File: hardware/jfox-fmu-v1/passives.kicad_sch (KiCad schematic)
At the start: 38 parts, among them X1 16MHz, X2 32.768kHz

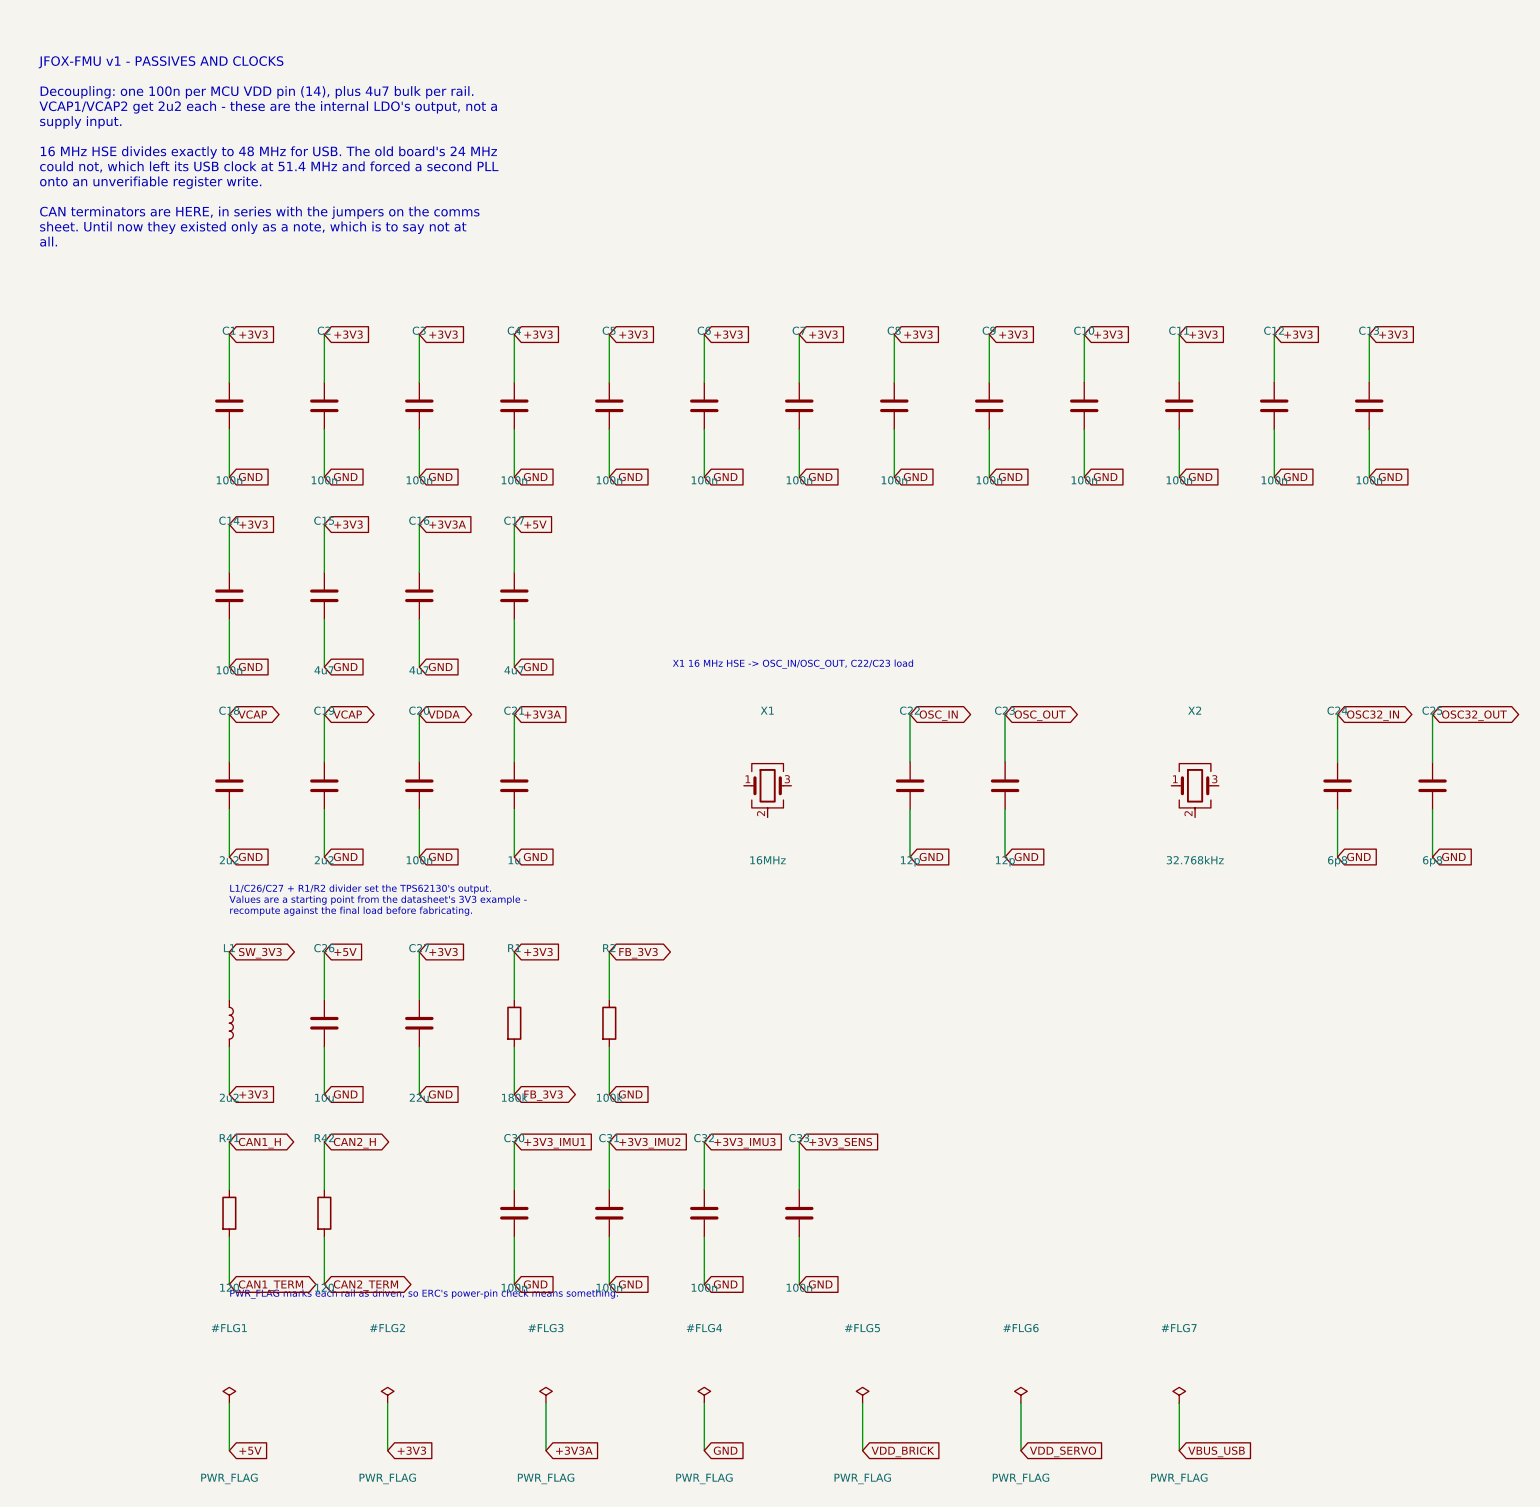
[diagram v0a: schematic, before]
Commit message: A4 title-blocked sheets, and the 25 power pins that were never wired
Every sheet now carries a title block naming JFOX Aircraft Co., Ltd., with a
per-sheet title, revision, date and the notes that used to float as loose text.

A4 PORTRAIT, not landscape, and not by preference. The STM32H753IITx symbol is
a single unit - KiCad's library gives it only _0_1 body and _1_1 pin
sub-symbols, so it cannot be split across pages - and its 176 pins span
231.1 mm. A4 landscape offers about 180 mm of usable height and would cut the
MCU in half. Portrait offers 237 mm. The part fits with 2 mm to spare, which
is why the page margin is 2 mm: it is the largest margin that still holds an
LQFP176, not a number chosen for looks.

The frame geometry was measured, not assumed - an empty A4 portrait sheet
plotted through kicad-cli, frame read off the SVG at 12,12 -> 198,285 with the
title block claiming x >= 90, y >= 253.

Three defects the work surfaced, in rising order of how much they mattered:

Every sheet had content at negative coordinates, off the page entirely, where
KiCad edits it happily and the plotter crops it away. Nothing had complained
because nothing was looking. fit() now translates each sheet into the drawable
area and refuses - loudly - to emit one that does not fit, because a schematic
that is silently cropped lies about the board.

fit() then passed the power sheet while its rightmost label sat 8.6 mm past
the frame. A global label's angle is the direction its CONNECTION faces, so
the text runs the opposite way; reading it the intuitive way put every
estimated extent on the wrong side of its anchor. That is worse than not
estimating: it reports "inside the frame" precisely when labels hang off it.
Caught by measuring KiCad's own plotted geometry instead of trusting the
estimate - which is what check_fmu_sheets.py now does on every sheet, with
--exclude-drawing-sheet so only the circuit is measured.

And centring the sheets by (SAFE_W - w) / 2 shifted every wire off th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
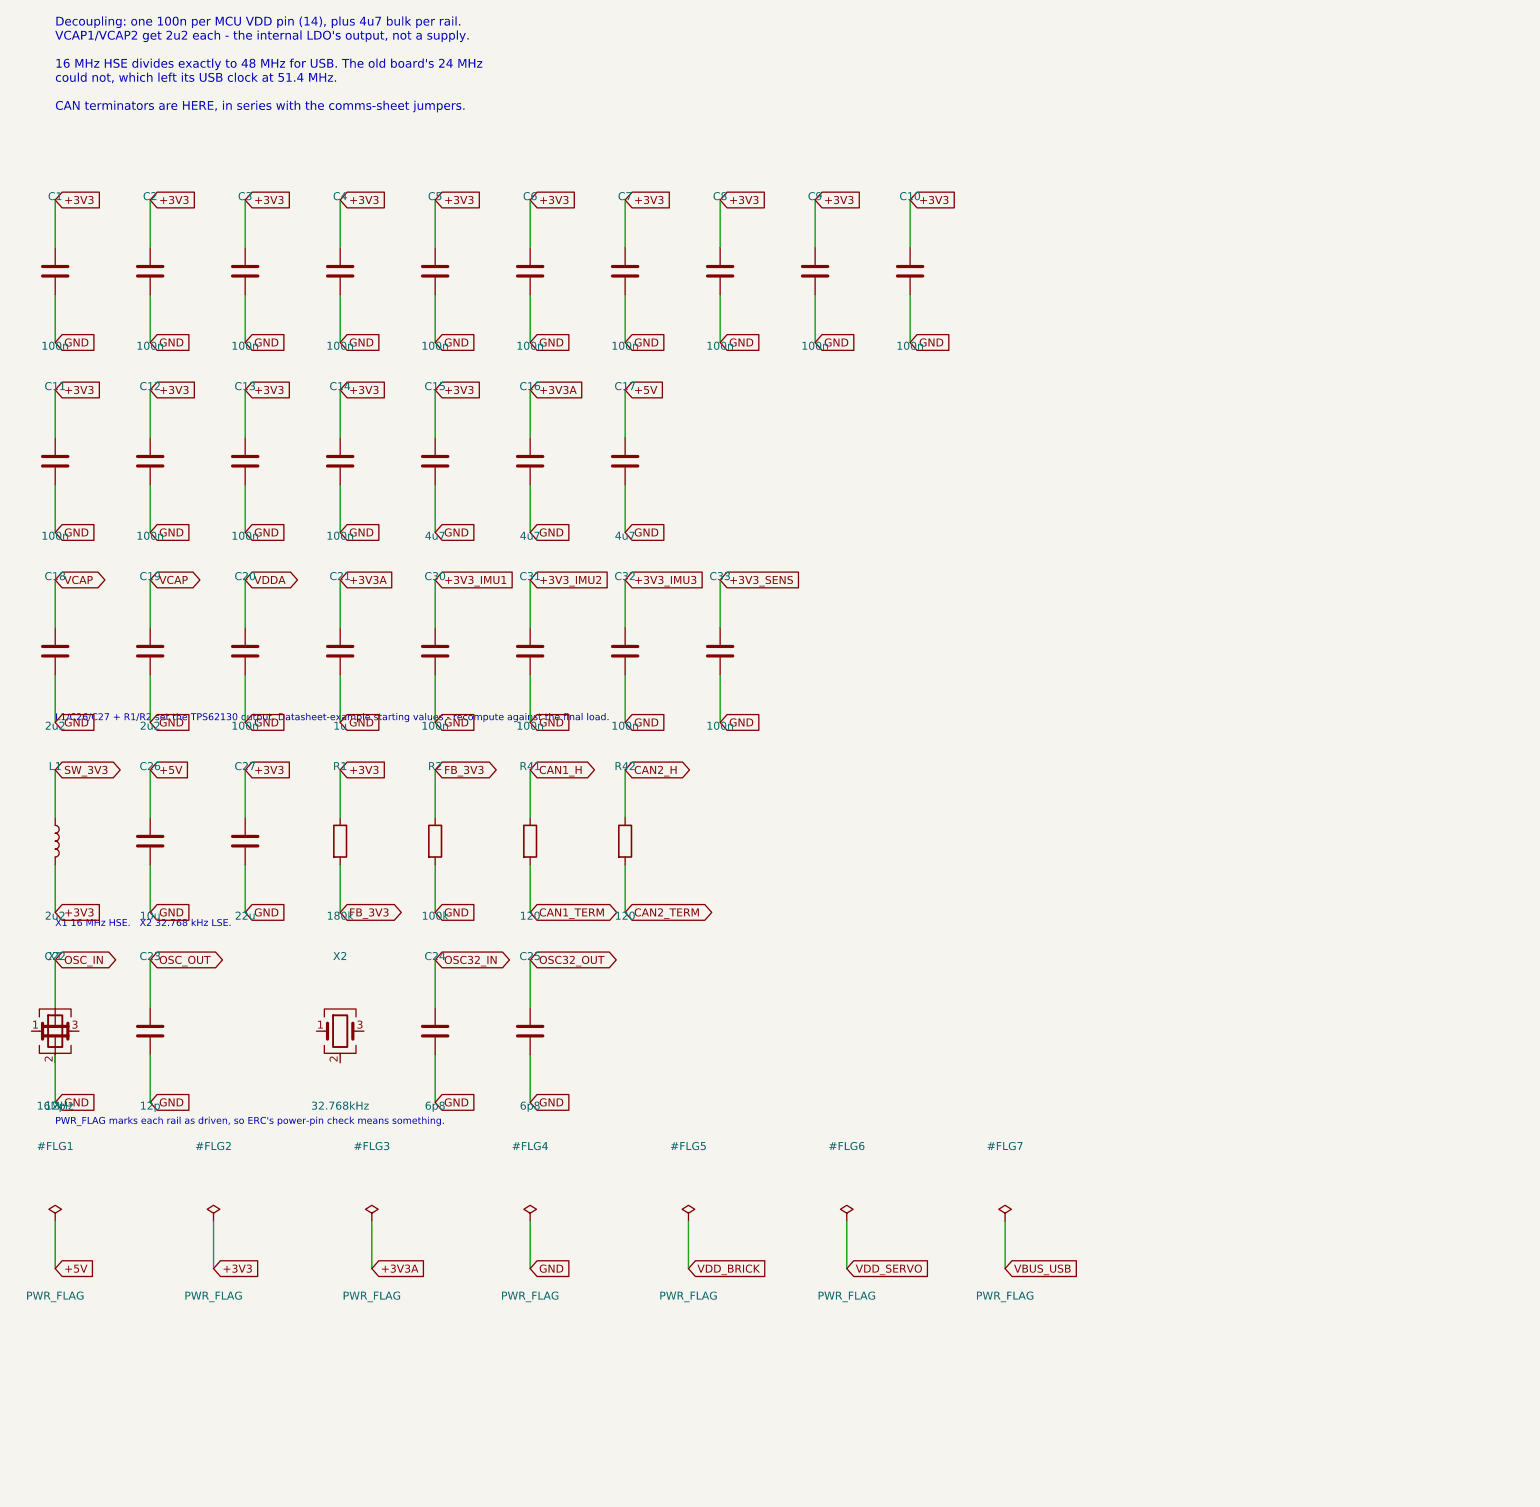
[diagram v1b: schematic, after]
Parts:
- X1, X2: footprint (none) -> Crystal:Crystal_SMD_3225-4Pin_3.2x2.5mm
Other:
- note added: "Decoupling: one 100n per MCU VDD pin (14), plus 4u7 bulk per rail. VCAP1/VCAP2 get 2u2 each - the internal LDO's output, not a supply. 16 MHz HSE divides exactly to 48 MHz for USB. The old board's 24 MHz could not, which left its USB clock at 51.4 MHz. CAN terminators are HERE, in series with the comms-sheet jumpers."
- note added: "L1/C26/C27 + R1/R2 set the TPS62130 output. Datasheet-example starting values - recompute against the final load."
- note added: "X1 16 MHz HSE. X2 32.768 kHz LSE."
- note removed: "JFOX-FMU v1 - PASSIVES AND CLOCKS Decoupling: one 100n per MCU VDD pin (14), plus 4u7 bulk per rail. VCAP1/VCAP2 get 2u2 each - these are the internal LDO's output, not a supply input. 16 MHz HSE divides exactly to 48 MHz for USB. The old board's 24 MHz could not, which left its USB clock at 51.4 MHz and forced a second PLL onto an unverifiable register write. CAN terminators are HERE, in series 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"
- note removed: "L1/C26/C27 + R1/R2 divider set the TPS62130's output. Values are a starting point from the datasheet's 3V3 example - recompute against the final load before fabricating."
- note removed: "X1 16 MHz HSE -> OSC_IN/OSC_OUT, C22/C23 load"
- company: (none) -> JFOX Aircraft Co., Ltd.
- title: (none) -> Passives and Clocks

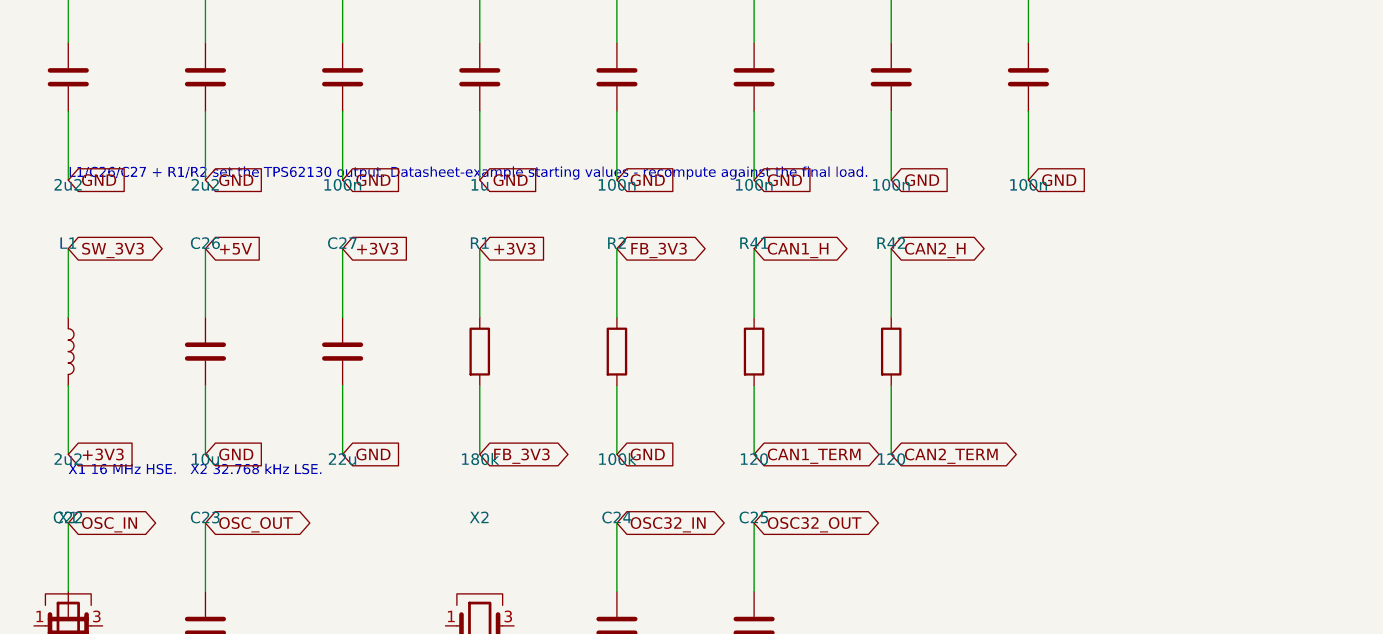
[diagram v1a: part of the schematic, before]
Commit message: U21 was set to 2.24 V, not 3.3 V
The 3V3 rail's regulator was an adjustable TPS62130 with a 180k/100k feedback
divider, carried in the schematic as "a starting point from the datasheet's
3V3 example". It was not a starting point. The TPS62130 regulates FB to 800 mV
(SLVSAG7F 9.2.2.1, equation 6), so 180k over 100k sets

    0.8 x (1 + 180/100) = 2.24 V

onto a net named +3V3. For 3.3 V the top resistor needed to be 312.5k.

Nothing caught this and nothing could have. ERC checks connectivity, not
arithmetic; the net was named +3V3 and every part was correctly connected to
it, so every structural check passed on a board that would have browned out
the STM32H753 and undervolted all three IMUs. The whole error was numbers,
and numbers were what nothing was looking at.

U21 becomes a TPS62132 - the fixed 3.3 V member of the same family, in the
same package, with a KiCad symbol already present. That removes the divider
instead of correcting it: two fewer parts, no divider tolerance stacking on
the reference, and the output voltage becomes a property of the ordering code
rather than something a resistor substitution can silently change.

Three parts the design was missing, all from the datasheet's own typical
application (figure 9-1): C28 100n on AVIN, C29 3n3 setting the soft-start
ramp, and R3 100k pulling up PG - which is open drain and was wired to a net
nothing on the board could drive.

L1 2u2 and C27 22u turn out to have been right all along, and now say why:
table 9-2 marks 2.2uH/22uF as the standard, recommended combination. FSW low
is 2.5 MHz for smallest size and lowest ripple; DEF low is nominal output; FB
goes to AGND as the datasheet asks for fixed versions.

check_fmu_schematic.py grows an eighth check: every rail must produce the
voltage its name claims. Fixed parts are verified by ordering code, adjustable
ones by computing Vfb x (1 + Rtop/Rbot) from the BOM values. Negative-tested
by restoring the 180k/100k divider, which it reports as 2.24 V, and by the
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
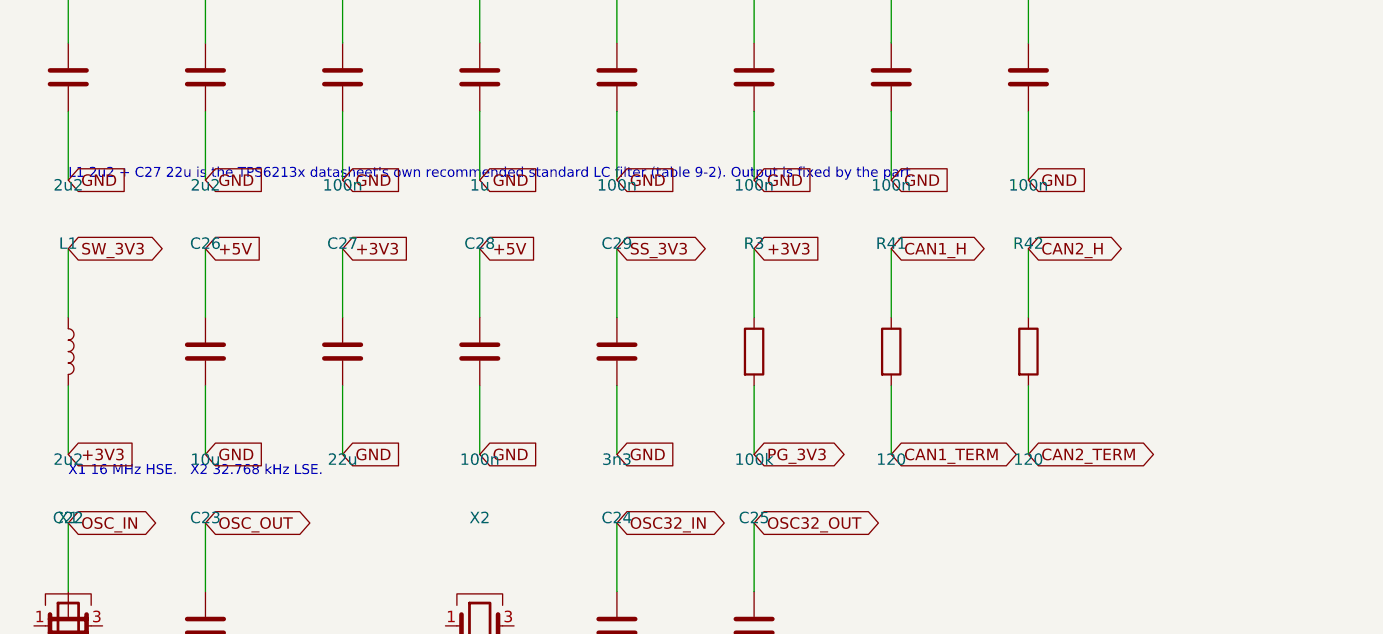
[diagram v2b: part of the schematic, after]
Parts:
- removed R1: 180k, symbol Device:R
- removed R2: 100k, symbol Device:R
- added C28: 100n, symbol Device:C
- added C29: 3n3, symbol Device:C
- added R3: 100k, symbol Device:R
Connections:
- net +3V3: now also R3.1
- net +5V: now also C28.1
- net GND: now also C28.2, C29.2
- new net PG_3V3: R3.2
- new net SS_3V3: C29.1
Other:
- note added: "L1 2u2 + C27 22u is the TPS6213x datasheet's own recommended standard LC filter (table 9-2). Output is fixed by the part."
- note removed: "L1/C26/C27 + R1/R2 set the TPS62130 output. Datasheet-example starting values - recompute against the final load."

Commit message: Footprint every part, and verify each one exists
58 of 58 components now carry a footprint chosen against the package its
datasheet specifies, and check_fmu_footprints.py confirms every name resolves
to a file on disk.

Three of the names this design was carrying did not. The symbol library named
`Sensor_Motion:InvenSense_QFN-14_3x3mm_P0.5mm` and
`Sensor_Pressure:Bosch_LGA-10_2x2mm_P0.35mm`, neither of which is a footprint
in any installed library - both plausible, both fiction. The third was worse:
`Package_LGA:Bosch_LGA-14_3x2.5mm_P0.5mm` is real, matches the InvenSense
package on every word of its name, and is drawn for the BMI160 with 0.675 mm
pads where InvenSense wants 0.475 mm.

Notable choices, each traceable:
  LTC4417CGN  GN is the 16-lead narrow SSOP.
  TPS62132    RGT 3x3 VQFN. TI's land drawing (4222419/E) gives the exposed
              pad as 1.55 mm; KiCad's 1.6 mm variant is closest. Thermal-via
              variant, since the datasheet is explicit that the pad must be
              soldered and that dissipation limits output power.
  Bulk caps   4u7/10u/22u get an 0805, not the 0402 every other capacitor
              gets. Assigning one size to all of them produces a board that
              cannot be built from the BOM it ships with.
  L1          a generic 1210 land, and labelled as such - the 2.2 uH part is
              not chosen yet, since saturation current and DCR still have to
              be picked against the real 550 mA peak.

The checker was wrong on its first run, in a way worth recording because the
failure mode is self-concealing. It matched ref, value and footprint in one
regex with the footprint group optional, so a component with no footprint -
precisely what it exists to find - failed to match at all, dropped out of the
list, and the run reported "every component maps to a footprint" while the
count quietly fell by one. A check whose failure mode is to stop seeing the
failure is worse than no check. Now it splits into per-com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
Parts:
- C1, C10, C11, C12, C13, C14, C18, C19, C2, C20, C21, C22, C23, C24, C25, C28, C29, C3, C30, C31, C32, C33, C4, C5, C6, C7, C8, C9: footprint (none) -> Capacitor_SMD:C_0402_1005Metric
- C15, C16, C17, C26, C27: footprint (none) -> Capacitor_SMD:C_0805_2012Metric
- L1: footprint (none) -> Inductor_SMD:L_1210_3225Metric
- R3, R41, R42: footprint (none) -> Resistor_SMD:R_0402_1005Metric
